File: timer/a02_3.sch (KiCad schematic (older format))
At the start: 23 parts, among them U24 74HC27, U25 74HC02, U26 74HC02, U27 74HC02, U28 74HC27, U29 74HC02, U30 74HC02, U31 74HC27, U32 74HC02, U33 74HC02, U34 74HC27, U35 74HC02, U36 74HC02, U37 74HC02, U38 74HC27, U39 74LVC07, U40 74HC04, U41 74HC04, U42 74HC04, U43 74HC04, U44 74HC27, U45 74HC04

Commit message: Renamed components in the timer module to fit the new numbering scheme (module_number * 1000 + part number), and updated initial conditions to make simulation happy again after fixes
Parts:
- renumbered R2 to R2002, U24 to U2024, U25 to U2025, U26 to U2026, U27 to U2027, U28 to U2028, U29 to U2029, U30 to U2030, U31 to U2031, U32 to U2032, U33 to U2033, U34 to U2034, U35 to U2035, U36 to U2036, U37 to U2037, U38 to U2038, U39 to U2039, U40 to U2040, U41 to U2041, U42 to U2042, U43 to U2043, U44 to U2044, U45 to U2045

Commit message: Added the 'stage' bit of the Stage Branch Decoder module, and cleaned up a lot of initial conditions (still probably a lot to be done there)
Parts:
- U2024, U2025, U2026, U2027, U2029, U2030, U2032, U2033, U2035, U2036: Initial (none) -> 1
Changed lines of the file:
@@
 F 2 "" H 3200 1250 60  0000 C CNN
 F 3 "" H 3200 1250 60  0000 C CNN
+F 4 "1" H 3450 1250 60  0000 C CIN "Initial"
 	1    3200 1250
 	1    0    0    -1
@@
 F 2 "" H 6050 1250 60  0000 C CNN
 F 3 "" H 6050 1250 60  0000 C CNN
+F 4 "1" H 6300 1250 60  0000 C CIN "Initial"
 	4    6050 1250
 	1    0    0    -1
@@
 F 2 "" H 8900 1250 60  0000 C CNN
 F 3 "" H 8900 1250 60  0000 C CNN
+F 4 "1" H 9150 1250 60  0000 C CIN "Initial"
 	3    8900 1250
 	1    0    0    -1
@@
 F 2 "" H 11750 1250 60  0000 C CNN
 F 3 "" H 11750 1250 60  0000 C CNN
+F 4 "1" H 12000 1250 60  0000 C CIN "Initial"
 	2    11750 1250
 	1    0    0    -1
@@
 F 2 "" H 14600 1250 60  0000 C CNN
 F 3 "" H 14600 1250 60  0000 C CNN
+F 4 "1" H 14850 1250 60  0000 C CIN "Initial"
 	1    14600 1250
 	1    0    0    -1
@@
 F 2 "" H 17450 1250 60  0000 C CNN
 F 3 "" H 17450 1250 60  0000 C CNN
+F 4 "1" H 17700 1250 60  0000 C CIN "Initial"
 	4    17450 1250
 	1    0    0    -1
@@
 F 2 "" H 3200 7600 60  0000 C CNN
 F 3 "" H 3200 7600 60  0000 C CNN
+F 4 "1" H 3450 7600 60  0000 C CIN "Initial"
 	3    3200 7600
 	1    0    0    -1
@@
 F 2 "" H 6050 7600 60  0000 C CNN
 F 3 "" H 6050 7600 60  0000 C CNN
+F 4 "1" H 6300 7600 60  0000 C CIN "Initial"
 	2    6050 7600
 	1    0    0    -1
@@
 F 2 "" H 8900 7600 60  0000 C CNN
 F 3 "" H 8900 7600 60  0000 C CNN
+F 4 "1" H 9150 7600 60  0000 C CIN "Initial"
 	1    8900 7600
 	1    0    0    -1
@@
 F 2 "" H 11750 7600 60  0000 C CNN
 F 3 "" H 11750 7600 60  0000 C CNN
+F 4 "1" H 12000 7600 60  0000 C CIN "Initial"
 	4    11750 7600
 	1    0    0    -1
@@
 F 2 "" H 14600 7600 60  0000 C CNN
 F 3 "" H 14600 7600 60  0000 C CNN
+F 4 "1" H 14850 7600 60  0000 C CIN "Initial"
 	3    14600 7600
 	1    0    0    -1
@@
 F 2 "" H 17600 7600 60  0000 C CNN
 F 3 "" H 17600 7600 60  0000 C CNN
+F 4 "1" H 17850 7600 60  0000 C CIN "Initial"
 	2    17600 7600
 	1    0    0    -1

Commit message: Tied in module 8, and corrected lots of initial conditions.
The registers and ALU appear to work now, with TC0 and STD2 shuffling things around correctly, and Z counting up as instructions execute.
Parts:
- U2040, U2041, U2042, U2043: Initial (none) -> 1
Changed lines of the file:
@@
 F 2 "" H 3150 8900 60  0000 C CNN
 F 3 "" H 3150 8900 60  0000 C CNN
+F 4 "1" H 3200 8900 60  0000 C CIN "Initial"
 	1    3150 8900
 	1    0    0    -1
@@
 F 2 "" H 3150 9400 60  0000 C CNN
 F 3 "" H 3150 9400 60  0000 C CNN
+F 4 "1" H 3200 9400 60  0000 C CIN "Initial"
 	3    3150 9400
 	1    0    0    -1
@@
 F 2 "" H 3150 9900 60  0000 C CNN
 F 3 "" H 3150 9900 60  0000 C CNN
+F 4 "1" H 3200 9900 60  0000 C CIN "Initial"
 	5    3150 9900
 	1    0    0    -1
@@
 F 2 "" H 3150 10400 60  0000 C CNN
 F 3 "" H 3150 10400 60  0000 C CNN
+F 4 "1" H 3200 10400 60  0000 C CIN "Initial"
 	1    3150 10400
 	1    0    0    -1
@@
 F 2 "" H 3150 10900 60  0000 C CNN
 F 3 "" H 3150 10900 60  0000 C CNN
+F 4 "1" H 3200 10900 60  0000 C CIN "Initial"
 	3    3150 10900
 	1    0    0    -1
@@
 F 2 "" H 3150 11400 60  0000 C CNN
 F 3 "" H 3150 11400 60  0000 C CNN
+F 4 "1" H 3200 11400 60  0000 C CIN "Initial"
 	5    3150 11400
 	1    0    0    -1
@@
 F 2 "" H 6250 8900 60  0000 C CNN
 F 3 "" H 6250 8900 60  0000 C CNN
+F 4 "1" H 6300 8900 60  0000 C CIN "Initial"
 	1    6250 8900
 	1    0    0    -1
@@
 F 2 "" H 6250 9400 60  0000 C CNN
 F 3 "" H 6250 9400 60  0000 C CNN
+F 4 "1" H 6300 9400 60  0000 C CIN "Initial"
 	3    6250 9400
 	1    0    0    -1
@@
 F 2 "" H 6250 9900 60  0000 C CNN
 F 3 "" H 6250 9900 60  0000 C CNN
+F 4 "1" H 6300 9900 60  0000 C CIN "Initial"
 	5    6250 9900
 	1    0    0    -1
@@
 F 2 "" H 6250 10400 60  0000 C CNN
 F 3 "" H 6250 10400 60  0000 C CNN
+F 4 "1" H 6300 10400 60  0000 C CIN "Initial"
 	1    6250 10400
 	1    0    0    -1
@@
 F 2 "" H 6250 10900 60  0000 C CNN
 F 3 "" H 6250 10900 60  0000 C CNN
+F 4 "1" H 6300 10900 60  0000 C CIN "Initial"
 	3    6250 10900
 	1    0    0    -1
@@
 F 2 "" H 6250 11400 60  0000 C CNN
 F 3 "" H 6250 11400 60  0000 C CNN
+F 4 "1" H 6300 11400 60  0000 C CIN "Initial"
 	5    6250 11400
 	1    0    0    -1

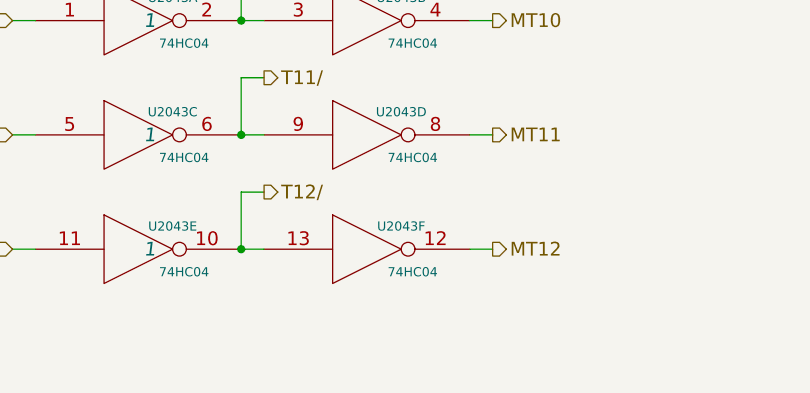
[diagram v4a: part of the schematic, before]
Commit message: Added and tied in module 12, parity & s register
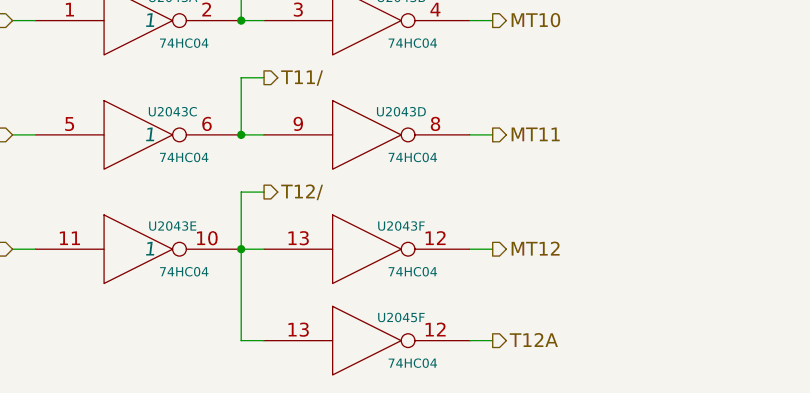
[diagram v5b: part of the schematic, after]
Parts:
- added unit 6 of U2045
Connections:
- net GND: now also U2045.7 (GND)
- net T12/: now also U2045.13
- net VCC: now also U2045.14 (VCC)
- new net T12A: U2045.12
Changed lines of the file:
@@
 	6800 11150 6700 11150
 Wire Wire Line
-	6700 11150 6700 11400
+	6700 11150 6700 11800
 Connection ~ 6700 11400
 Wire Wire Line
@@
 Wire Wire Line
 	10950 10150 11100 10150
+$Comp
+L 74HC04 U2045
+U 6 1 56E86F2E
+P 7250 11800
+F 0 "U2045" H 7400 11900 40  0000 C CNN
+F 1 "74HC04" H 7450 11700 40  0000 C CNN
+F 2 "" H 7250 11800 60  0000 C CNN
+F 3 "" H 7250 11800 60  0000 C CNN
+	6    7250 11800
+	1    0    0    -1
+$EndComp
+Wire Wire Line
+	6700 11800 6800 11800
+Wire Wire Line
+	7700 11800 7800 11800
+Text HLabel 7800 11800 2    60   Output ~ 0
+T12A
 $EndSCHEMATC

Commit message: SUPER BROKEN: Pulled in all NOR gates into the custom library, and changed the shape of 74HC04. Some, but not all, gates have standalone power pin parts. Scaler and Timer have been updated to use the new lib and rearranged to fit the new NOTs.
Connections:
- wire segments 391 -> 393
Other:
- moved on the sheet: U2040A, U2040B, U2040C, U2040D, U2040E, U2040F, U2041A, U2041B, U2041C, U2041D, U2041E, U2041F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
